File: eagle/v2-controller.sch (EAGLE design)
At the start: 16 parts, among them Q1 DHT##, Q2 RS485-ADAPTER0.05-CONNECTOR, X1 RJ45-6L21-B

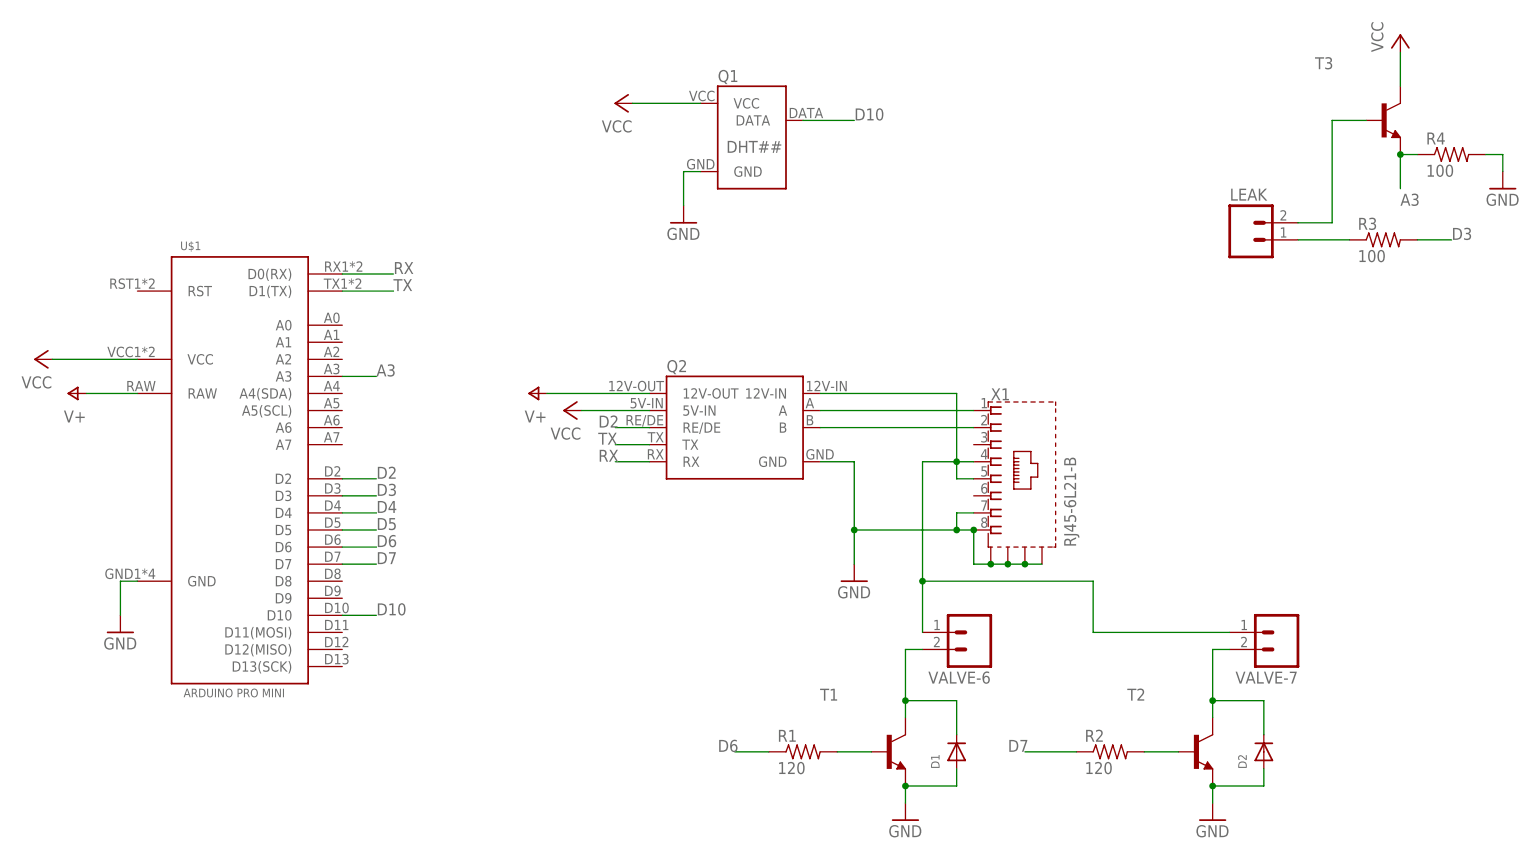
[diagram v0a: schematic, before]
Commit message: Moving v2 sprinkler board controls to the same location. Adding a buzzed for alerting when water leak is detected.
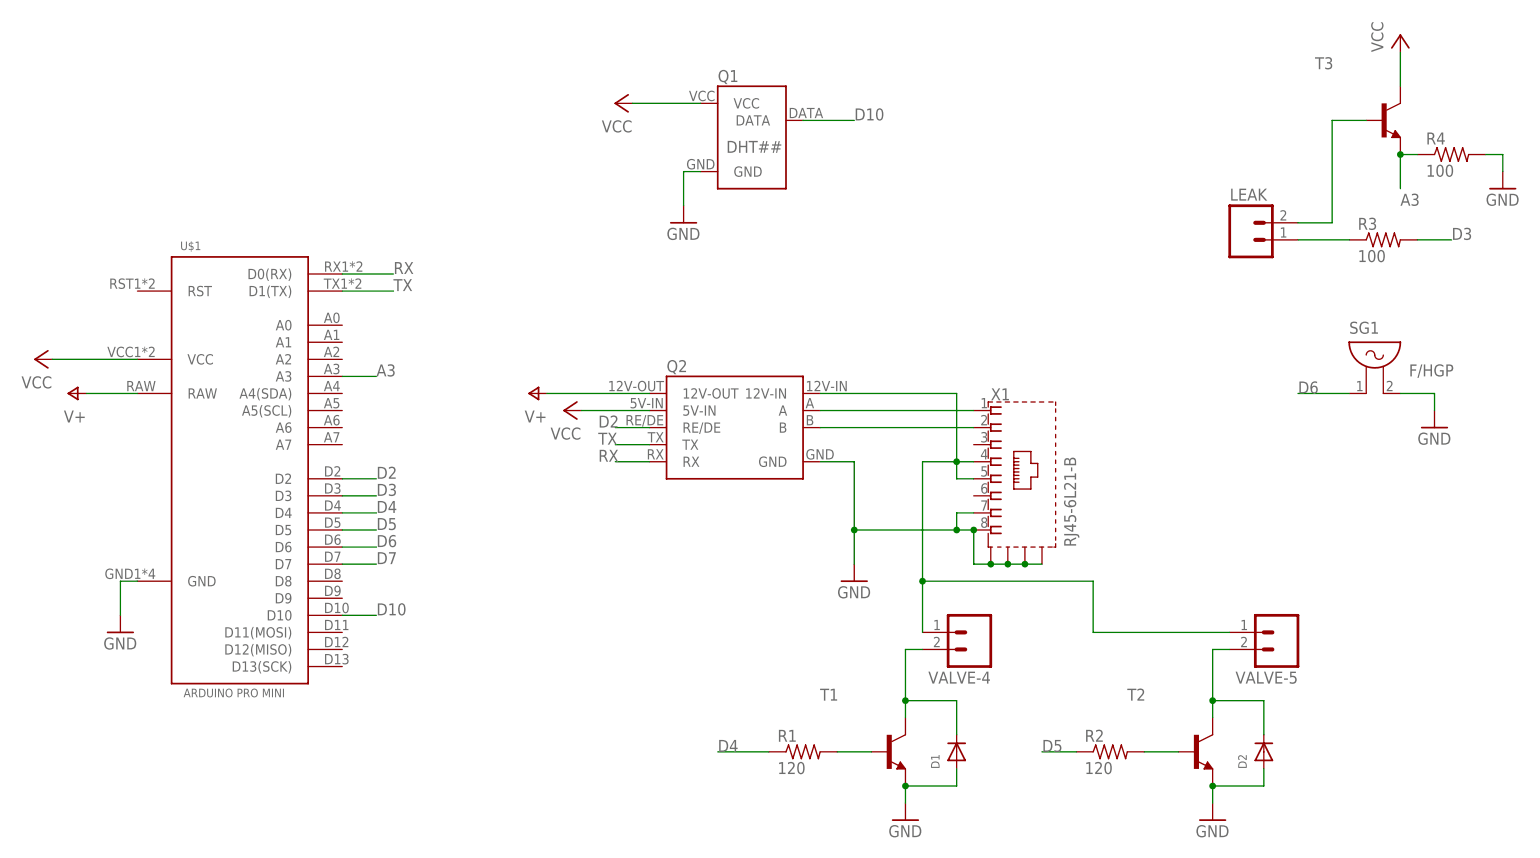
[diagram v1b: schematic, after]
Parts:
- added SG1: F/HGP, buzzer:F/HGP
- renumbered VALVE-6 to VALVE-4, VALVE-7 to VALVE-5
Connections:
- net D4: now also R1.1
- net D5: now also R2.1
- net D6: now also SG1.1; no longer R1.1
- net D7: no longer R2.1
- net GND: now also SG1.2
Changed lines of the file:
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@@
 <part name="T1" library="transistor" deviceset="*-NPN-" device="SOT23-BEC" technology="BC808"/>
 <part name="D1" library="adafruit" deviceset="DIODE" device="SMA"/>
-<part name="VALVE-6" library="con-amp-quick" deviceset="M02" device=""/>
+<part name="VALVE-4" library="con-amp-quick" deviceset="M02" device=""/>
 <part name="Q1" library="serge" deviceset="DHT##" device=""/>
 <part name="P+5" library="supply1" deviceset="VCC" device=""/>
@@
 <part name="T2" library="transistor" deviceset="*-NPN-" device="SOT23-BEC" technology="BC808"/>
 <part name="D2" library="adafruit" deviceset="DIODE" device="SMA"/>
-<part name="VALVE-7" library="con-amp-quick" deviceset="M02" device=""/>
+<part name="VALVE-5" library="con-amp-quick" deviceset="M02" device=""/>
 <part name="GND6" library="supply1" deviceset="GND" device=""/>
 <part name="Q2" library="serge" deviceset="RS485-ADAPTER" device="0.05-CONNECTOR"/>
@@
 <part name="GND7" library="supply1" deviceset="GND" device=""/>
 <part name="P+8" library="supply1" deviceset="VCC" device=""/>
+<part name="SG1" library="buzzer" deviceset="F/HGP" device=""/>
+<part name="GND5" library="supply1" deviceset="GND" device=""/>
 </parts>
 <sheets>
@@
 <instance part="T1" gate="G$1" x="116.84" y="20.32"/>
 <instance part="D1" gate="G$1" x="127" y="20.32" rot="R90"/>
-<instance part="VALVE-6" gate="G$1" x="129.54" y="38.1" rot="R180"/>
+<instance part="VALVE-4" gate="G$1" x="129.54" y="38.1" rot="R180"/>
 <instance part="Q1" gate="G$1" x="96.52" y="111.76"/>
 <instance part="P+5" gate="VCC" x="76.2" y="116.84" rot="R90"/>
@@
 <instance part="T2" gate="G$1" x="162.56" y="20.32"/>
 <instance part="D2" gate="G$1" x="172.72" y="20.32" rot="R90"/>
-<instance part="VALVE-7" gate="G$1" x="175.26" y="38.1" rot="R180"/>
+<instance part="VALVE-5" gate="G$1" x="175.26" y="38.1" rot="R180"/>
 <instance part="GND6" gate="1" x="165.1" y="10.16"/>
 <instance part="Q2" gate="G$1" x="88.9" y="71.12"/>
@@
 <instance part="GND7" gate="1" x="208.28" y="104.14"/>
 <instance part="P+8" gate="VCC" x="193.04" y="127"/>
+<instance part="SG1" gate="G$1" x="187.96" y="76.2"/>
+<instance part="GND5" gate="1" x="198.12" y="68.58"/>
 </instances>
 <busses>
@@
 <wire x1="127" y1="22.86" x2="127" y2="27.94" width="0.1524" layer="91"/>
 <wire x1="127" y1="27.94" x2="119.38" y2="27.94" width="0.1524" layer="91"/>
-<pinref part="VALVE-6" gate="G$1" pin="2"/>
+<pinref part="VALVE-4" gate="G$1" pin="2"/>
 <wire x1="121.92" y1="35.56" x2="119.38" y2="35.56" width="0.1524" layer="91"/>
 <wire x1="119.38" y1="35.56" x2="119.38" y2="27.94" width="0.1524" layer="91"/>
@@
 <wire x1="208.28" y1="109.22" x2="208.28" y2="106.68" width="0.1524" layer="91"/>
 </segment>
+<segment>
+<pinref part="SG1" gate="G$1" pin="2"/>
+<pinref part="GND5" gate="1" pin="GND"/>
+<wire x1="193.04" y1="73.66" x2="198.12" y2="73.66" width="0.1524" layer="91"/>
+<wire x1="198.12" y1="73.66" x2="198.12" y2="71.12" width="0.1524" layer="91"/>
+</segment>
 </net>
 <net name="VCC" class="0">
@@
 <wire x1="127" y1="73.66" x2="127" y2="63.5" width="0.1524" layer="91"/>
 <wire x1="106.68" y1="73.66" x2="127" y2="73.66" width="0.1524" layer="91"/>
-<pinref part="VALVE-6" gate="G$1" pin="1"/>
+<pinref part="VALVE-4" gate="G$1" pin="1"/>
 <wire x1="127" y1="63.5" x2="121.92" y2="63.5" width="0.1524" layer="91"/>
 <wire x1="121.92" y1="63.5" x2="121.92" y2="45.72" width="0.1524" layer="91"/>
-<pinref part="VALVE-7" gate="G$1" pin="1"/>
+<pinref part="VALVE-5" gate="G$1" pin="1"/>
 <wire x1="121.92" y1="45.72" x2="121.92" y2="38.1" width="0.1524" layer="91"/>
 <wire x1="167.64" y1="38.1" x2="147.32" y2="38.1" width="0.1524" layer="91"/>
@@
 <wire x1="172.72" y1="22.86" x2="172.72" y2="27.94" width="0.1524" layer="91"/>
 <wire x1="172.72" y1="27.94" x2="165.1" y2="27.94" width="0.1524" layer="91"/>
-<pinref part="VALVE-7" gate="G$1" pin="2"/>
+<pinref part="VALVE-5" gate="G$1" pin="2"/>
 <wire x1="167.64" y1="35.56" x2="165.1" y2="35.56" width="0.1524" layer="91"/>
 <wire x1="165.1" y1="35.56" x2="165.1" y2="27.94" width="0.1524" layer="91"/>
@@
 <pinref part="U$1" gate="G$1" pin="D4"/>
 </segment>
+<segment>
+<pinref part="R1" gate="G$1" pin="1"/>
+<wire x1="99.06" y1="20.32" x2="91.44" y2="20.32" width="0.1524" layer="91"/>
+<label x="91.44" y="20.32" size="1.778" layer="95"/>
+</segment>
 </net>
 <net name="D5" class="0">
@@
 <label x="40.64" y="53.34" size="1.778" layer="95"/>
 <pinref part="U$1" gate="G$1" pin="D5"/>
+</segment>
+<segment>
+<pinref part="R2" gate="G$1" pin="1"/>
+<wire x1="144.78" y1="20.32" x2="139.7" y2="20.32" width="0.1524" layer="91"/>
+<label x="139.7" y="20.32" size="1.778" layer="95"/>
 </segment>
 </net>
@@
 </segment>
 <segment>
-<pinref part="R1" gate="G$1" pin="1"/>
-<wire x1="99.06" y1="20.32" x2="93.98" y2="20.32" width="0.1524" layer="91"/>
-<label x="91.44" y="20.32" size="1.778" layer="95"/>
+<pinref part="SG1" gate="G$1" pin="1"/>
+<wire x1="185.42" y1="73.66" x2="177.8" y2="73.66" width="0.1524" layer="91"/>
+<label x="177.8" y="73.66" size="1.778" layer="95"/>
 </segment>
 </net>
@@
 <label x="40.64" y="48.26" size="1.778" layer="95"/>
 </segment>
-<segment>
-<pinref part="R2" gate="G$1" pin="1"/>
-<wire x1="144.78" y1="20.32" x2="137.16" y2="20.32" width="0.1524" layer="91"/>
-<label x="134.62" y="20.32" size="1.778" layer="95"/>
-</segment>
-</net>
+</net>
